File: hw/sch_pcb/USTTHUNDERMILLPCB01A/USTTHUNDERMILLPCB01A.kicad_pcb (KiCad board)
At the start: 4 copper layers, 80 x 80 mm, 70 parts, among them J1 SM04B-GHS-TB, J2 SM03B-GHS-TB, J4 HEADER_2x03, J5 SM08B-GHS-TB, J6 SM06B-GHS-TB, SW1 KMT031 NGJ LHS C&K, U1 ISL21080DIH312Z-TK 1V25, U2 OPA314, U3 MIC5504-3.3YM5, U4 PCF8583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

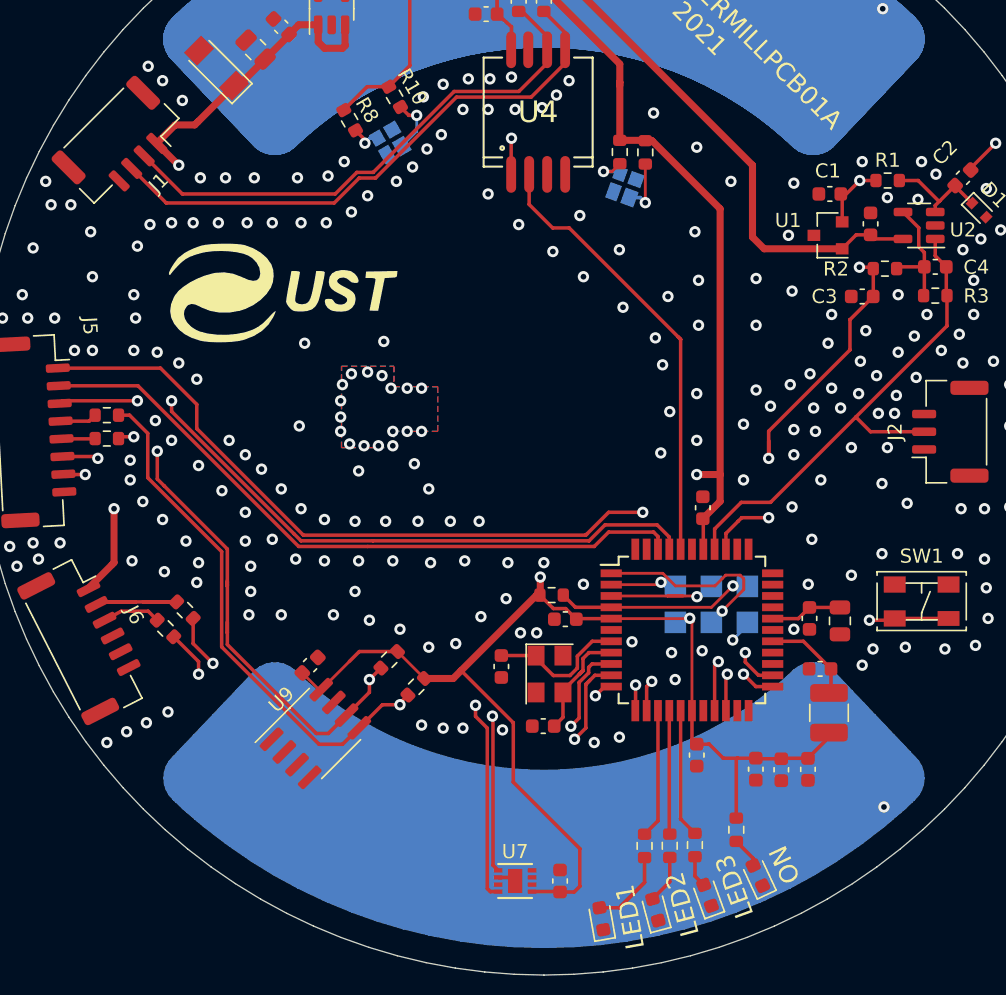
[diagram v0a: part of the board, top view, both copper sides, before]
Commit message: Clean layout of some tracks by using free-angle rounting.
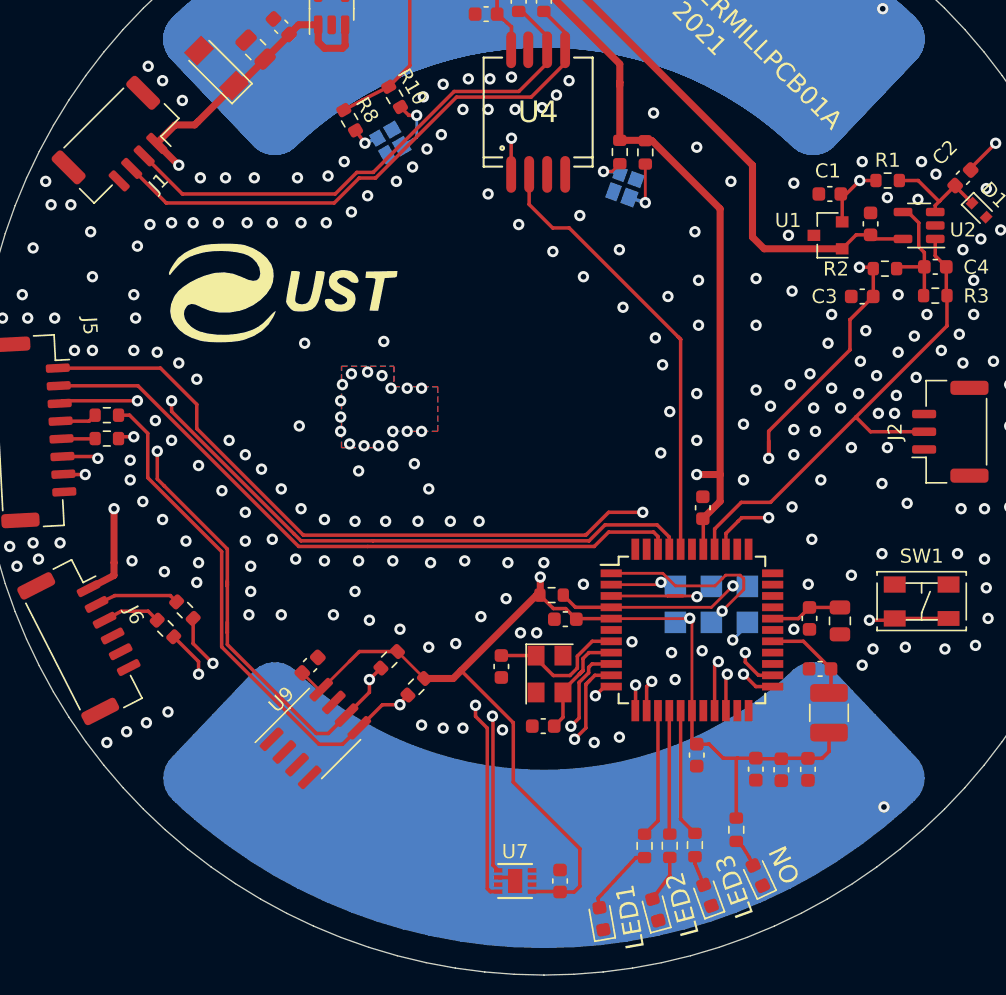
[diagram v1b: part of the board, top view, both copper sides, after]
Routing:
- net Net-(J6-Pad2): track 10.7 -> 6.58 mm
- net Net-(D4-Pad2): track 8.03 -> 5.22 mm

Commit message: Logo moved to the rotor window.
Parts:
- moved G*** 6.90 mm to (173.8, 94.1), turned to -92.1 degrees
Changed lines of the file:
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@@
   )
   (footprint "MLAB_LOGA:UST" (layer "B.Cu")
-    (at 166.878 93.98 180)
+    (at 173.775534 94.096071 -92.1)
     (attr through_hole)
-    (fp_text reference "G***" (at 0 0) (layer "B.SilkS") hide
+    (fp_text reference "G***" (at 0 0 87.9) (layer "B.SilkS") hide
       (effects (font (size 1.524 1.524) (thickness 0.3)) (justify mirror))
     )
-    (fp_text value "LOGO" (at 0.75 0) (layer "B.SilkS") hide
+    (fp_text value "LOGO" (at 0.75 0 87.9) (layer "B.SilkS") hide
       (effects (font (size 1.524 1.524) (thickness 0.3)) (justify mirror))
     )

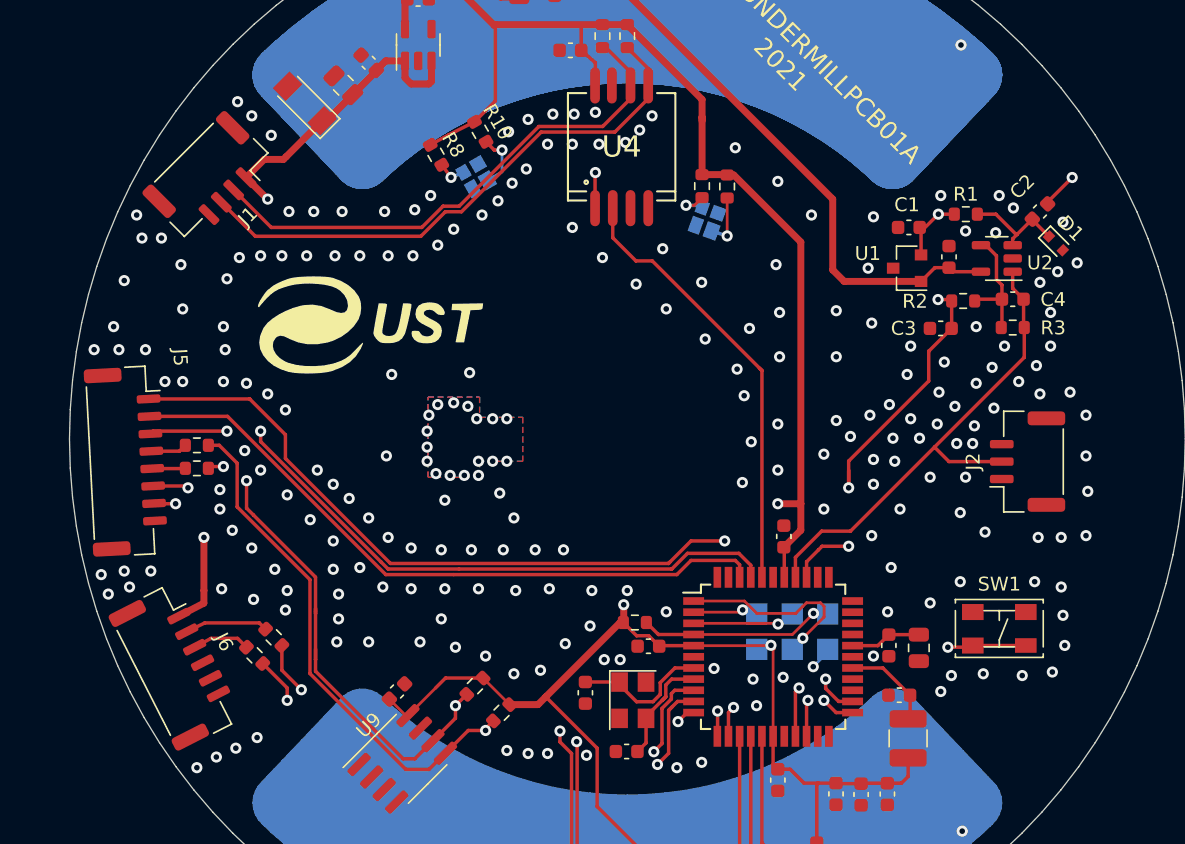
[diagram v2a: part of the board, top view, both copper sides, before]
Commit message: Move connectors.
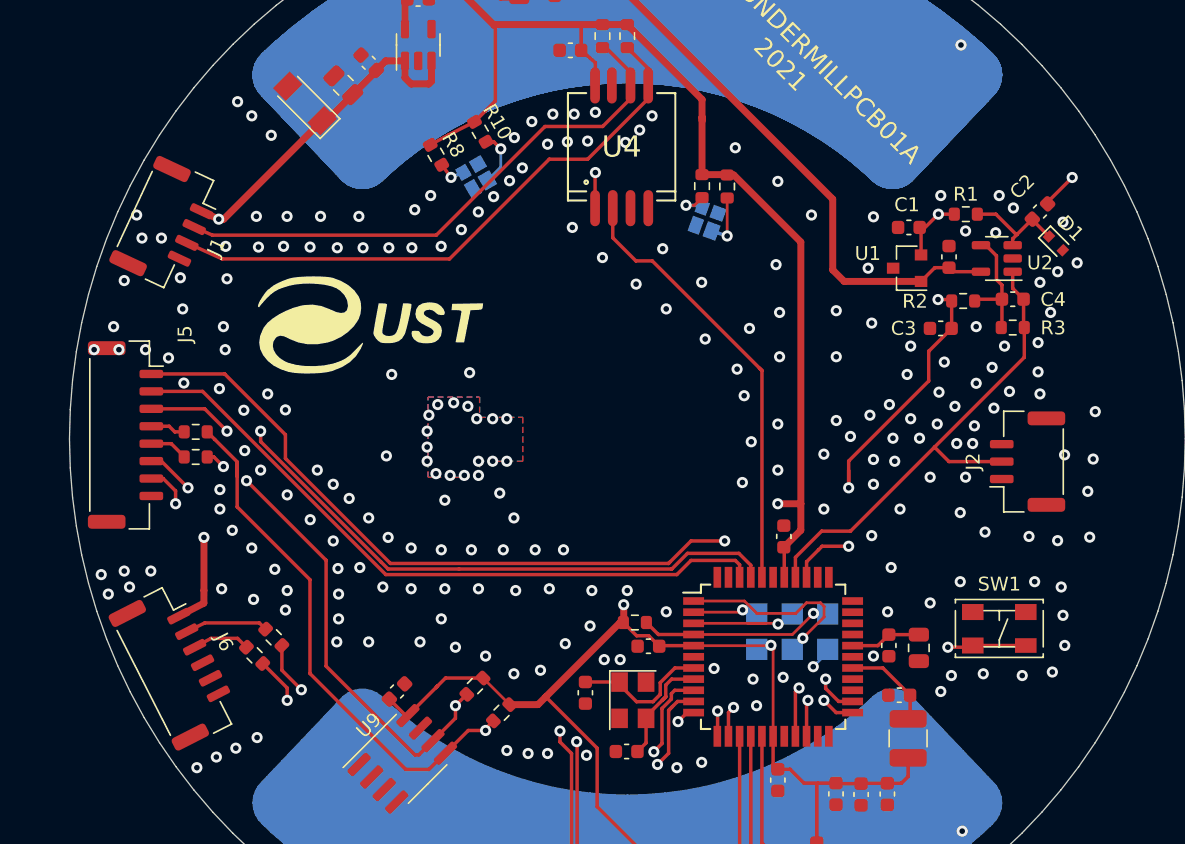
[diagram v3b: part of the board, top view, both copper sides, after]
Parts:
- moved J1 4.48 mm to (109.5, 77.1), turned to -115 degrees
- moved J5 1.88 mm to (106.5, 92.2), turned to -90 degrees
- moved R19 0.97 mm to (111.5, 92.0)
- moved R20 0.82 mm to (111.5, 93.8)
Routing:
- net /CPU/PC0: track 84.0 -> 80.2 mm
- net /tachometer/SDA: track 40.0 -> 42.4 mm
- net /tachometer/SCL: track 38.0 -> 40.1 mm
- net /CPU/PC1: track 75.7 -> 77.1 mm
- net /CPU/RX1: track 48.6 -> 50.0 mm
- net /CPU/TX1: track 52.8 -> 53.7 mm
- net /CPU/EXTINT: track 48.5 -> 49.1 mm
- net /CPU/TIMEPULSE: track 62.4 -> 63.0 mm
- net +5V: track 54.8 -> 54.3 mm
- net /CPU/GEO_STAT: track 49.3 -> 49.9 mm

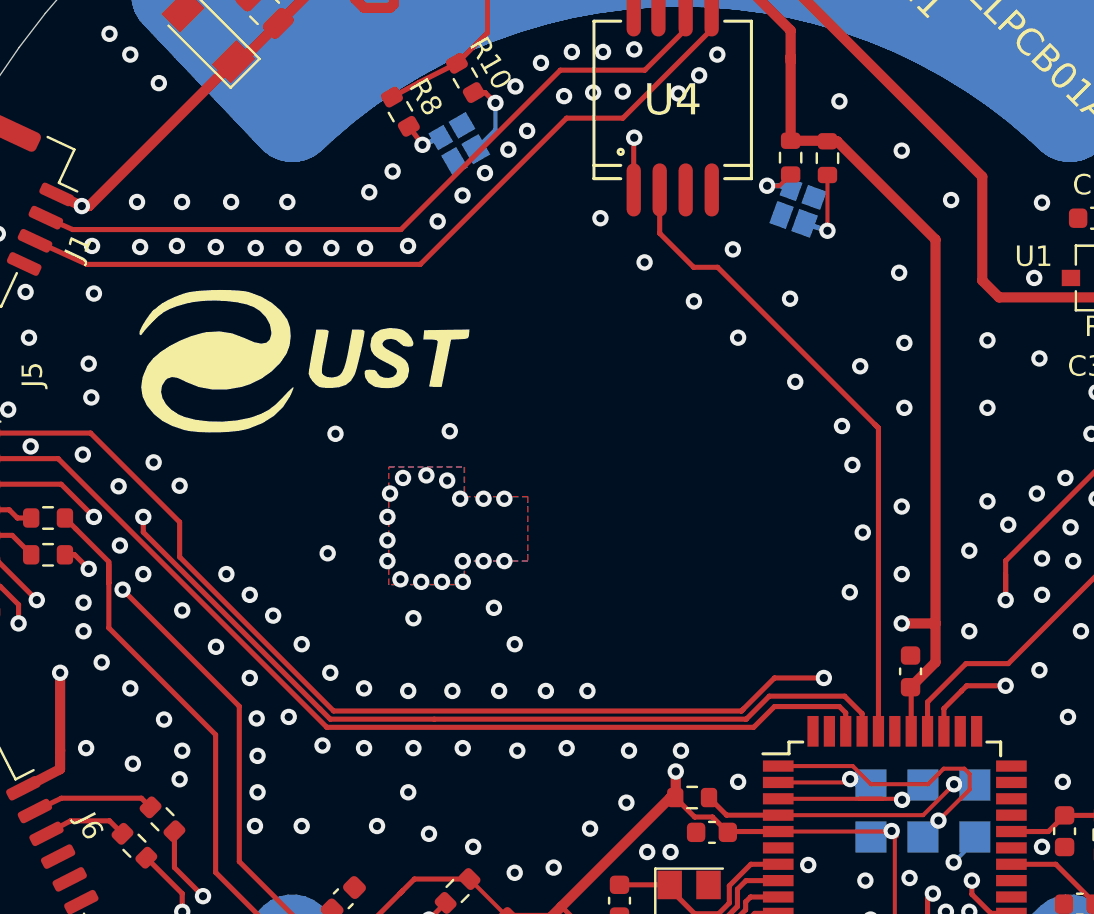
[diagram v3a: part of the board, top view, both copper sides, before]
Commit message: Silkscreen cleanup - DRC errors elimination.
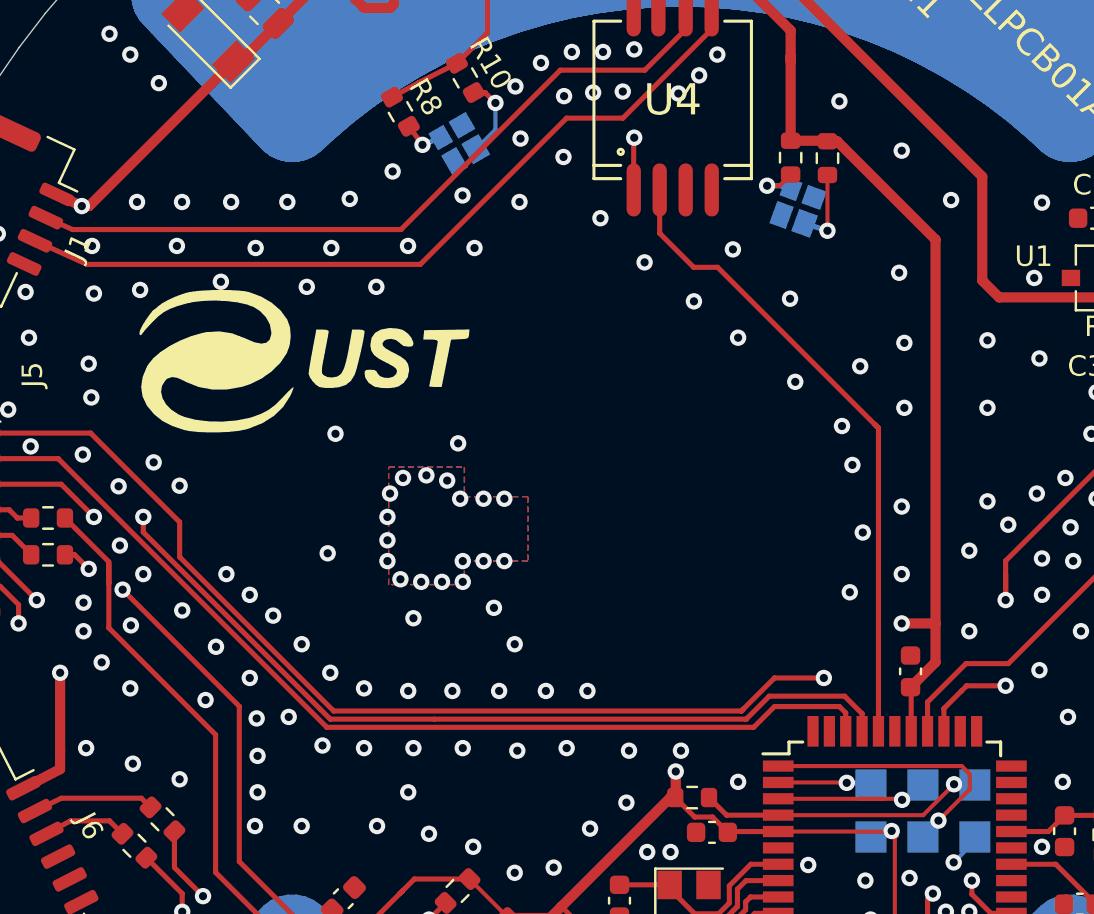
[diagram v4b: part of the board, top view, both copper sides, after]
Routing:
- net /CPU/PB5: track 13.1 -> 12.4 mm

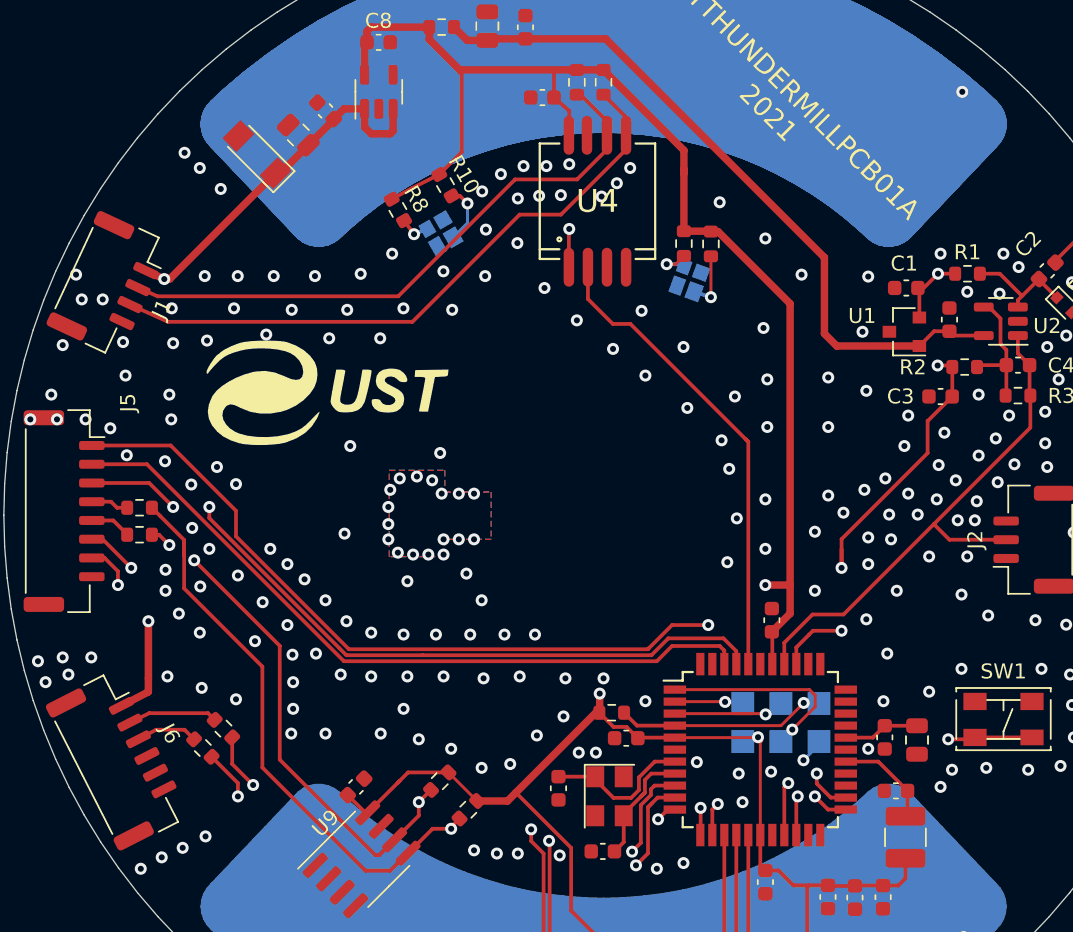
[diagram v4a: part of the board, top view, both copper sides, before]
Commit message: Eliminate some DRC errors.
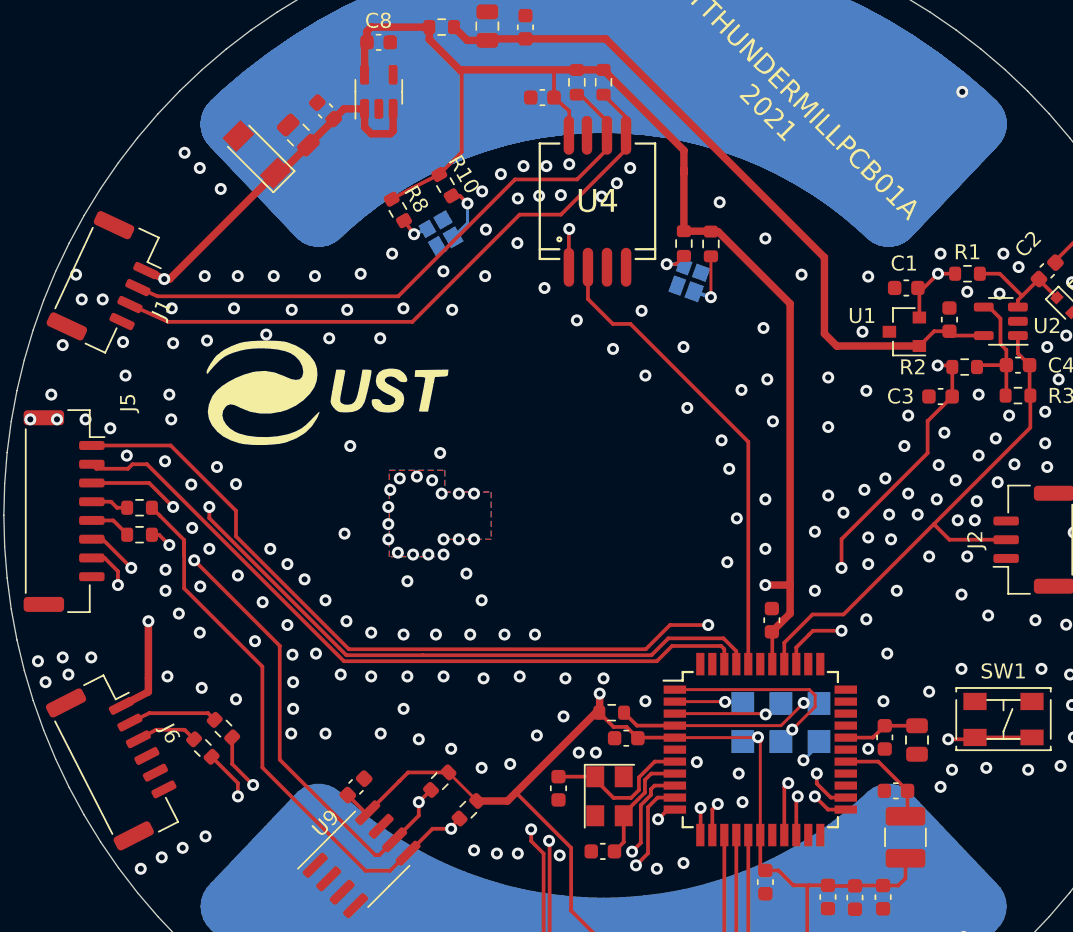
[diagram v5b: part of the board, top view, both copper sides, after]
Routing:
- net STATOR: track 137.6 -> 132.7 mm
- net +3V3: track 193.5 -> 191.5 mm
- net /CPU/PB7: track 8.49 -> 6.58 mm
- net PA1: track 38.5 -> 36.8 mm
- net /CPU/PC0: track 80.2 -> 79.3 mm
- net Net-(J6-Pad2): track 6.58 -> 5.99 mm
- net (no net): vias 1 -> 0
